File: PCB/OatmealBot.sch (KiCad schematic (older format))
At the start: 30 parts, among them J1 ServoHeader1, J10 ServoHeader3, J11 ServoHeader3, J12 ServoHeader3, J2 RPi_GPIO, J3 ServoHeader2, J4 ServoHeader1, J5 Motor 3, J6 Motor 4, J7 ServoHeader2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

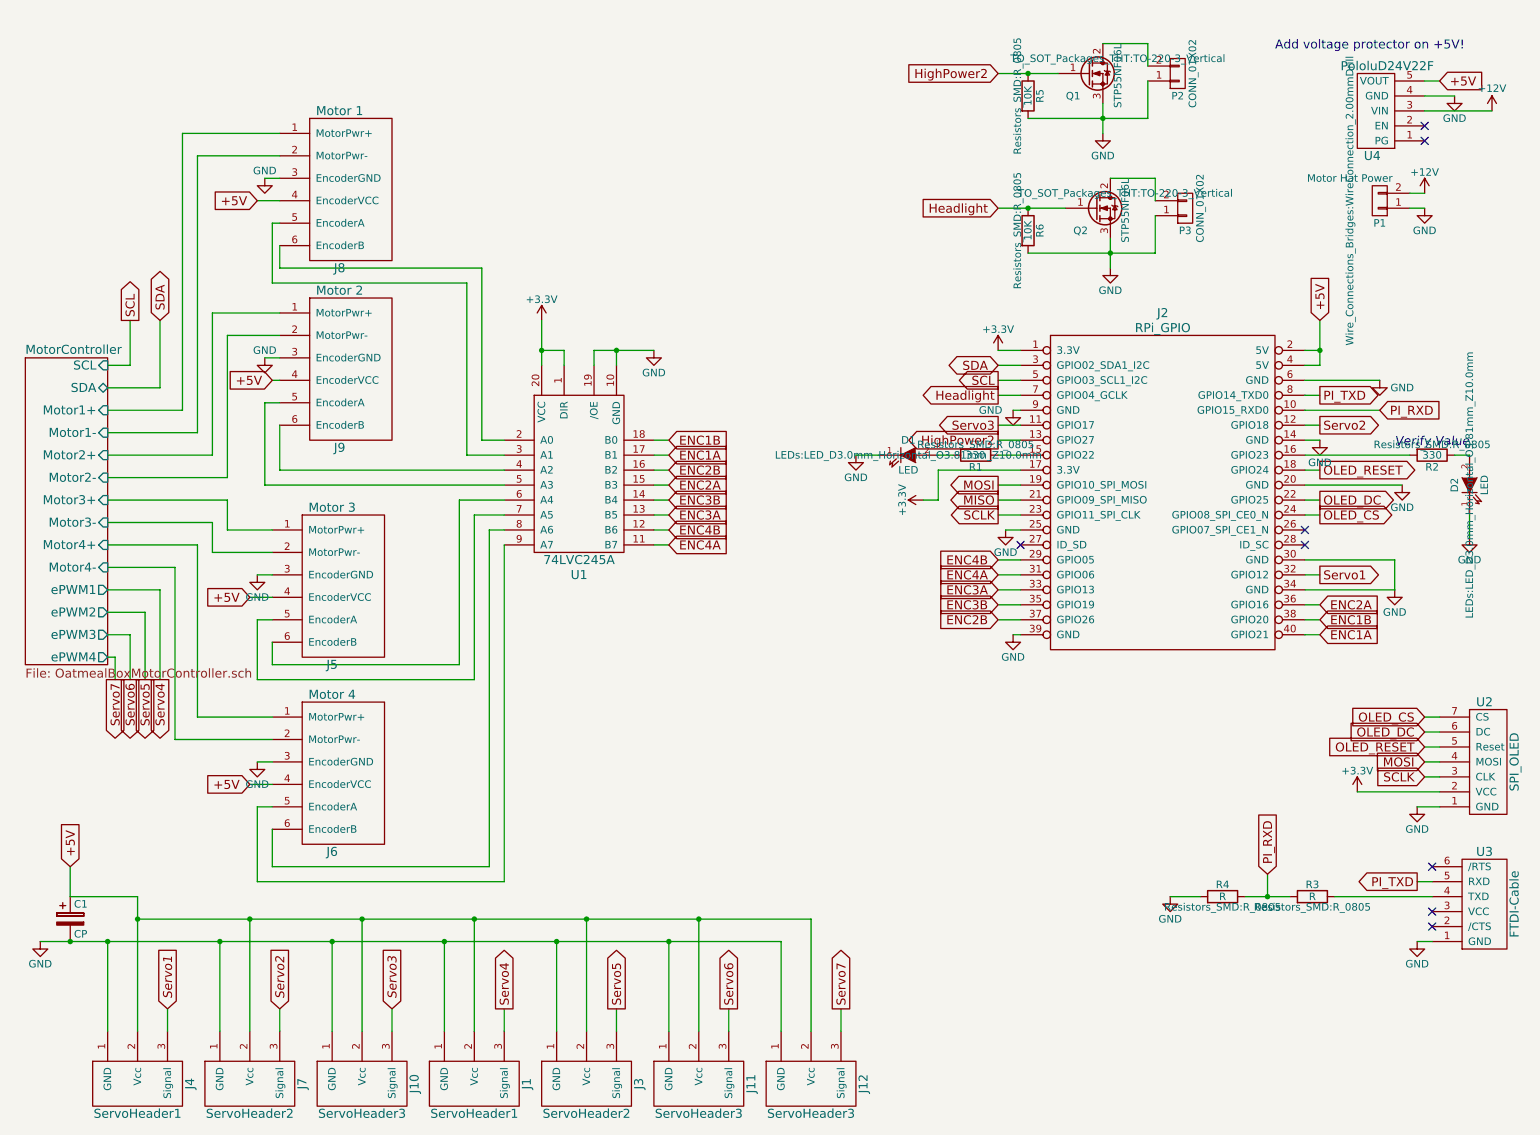
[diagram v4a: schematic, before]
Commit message: Cleaned up, renamed a few things and added all footprints.
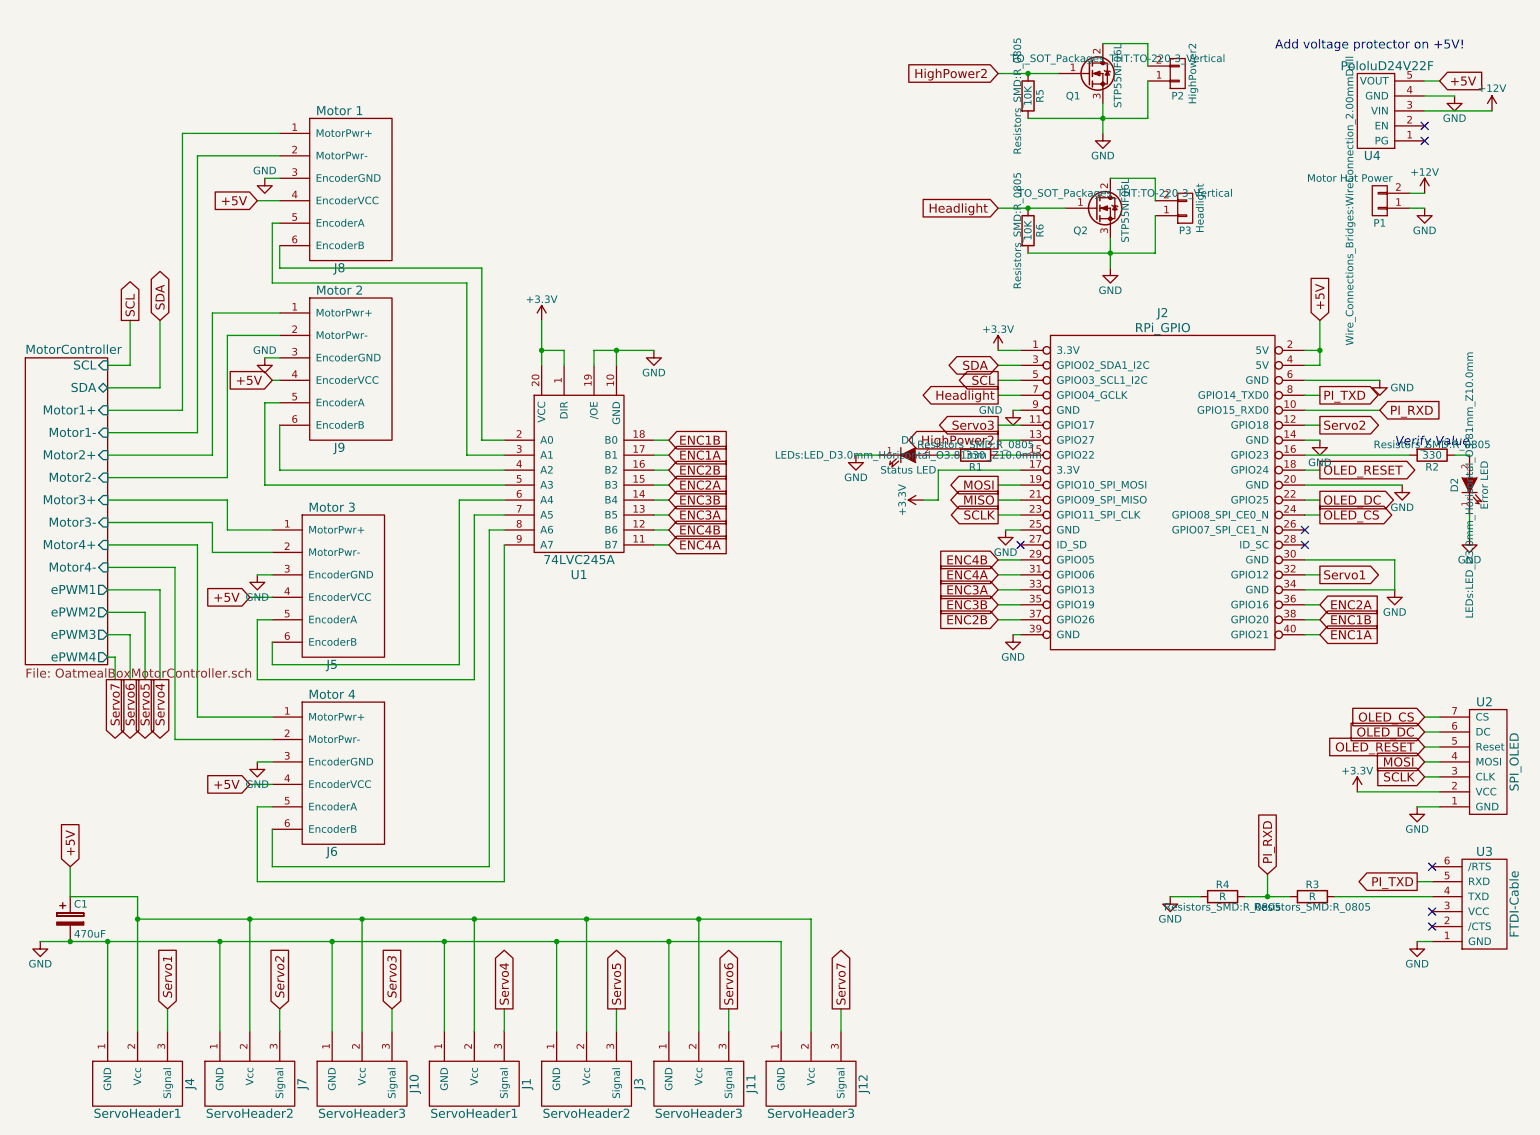
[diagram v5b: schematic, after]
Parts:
- C1: value CP -> 470uF; footprint (none) -> Capacitors_ThroughHole:CP_Radial_D12.5mm_P5.00mm
- D1: value LED -> Status LED
- D2: value LED -> Error LED
- P2: value CONN_01X02 -> HighPower2; footprint (none) -> Pin_Headers:Pin_Header_Straight_1x02_Pitch2.54mm
- P3: value CONN_01X02 -> Headlight; footprint (none) -> Pin_Headers:Pin_Header_Straight_1x02_Pitch2.54mm
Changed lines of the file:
@@
 +5V
 $Comp
-L GND #PWR4
+L GND #PWR01
 U 1 1 5B1F57E8
 P 2100 1450
-F 0 "#PWR4" H 2100 1200 50  0001 C CNN
+F 0 "#PWR01" H 2100 1200 50  0001 C CNN
 F 1 "GND" H 2100 1500 50  0000 C CNN
 F 2 "" H 2100 1450 50  0000 C CNN
@@
 +5V
 $Comp
-L GND #PWR5
+L GND #PWR02
 U 1 1 5B1F5859
 P 2100 2650
-F 0 "#PWR5" H 2100 2400 50  0001 C CNN
+F 0 "#PWR02" H 2100 2400 50  0001 C CNN
 F 1 "GND" H 2100 2700 50  0000 C CNN
 F 2 "" H 2100 2650 50  0000 C CNN
@@
 	1750 2350 2200 2350
 $Comp
-L GND #PWR3
+L GND #PWR03
 U 1 1 5B20546D
 P 2050 5350
-F 0 "#PWR3" H 2050 5100 50  0001 C CNN
+F 0 "#PWR03" H 2050 5100 50  0001 C CNN
 F 1 "GND" H 2050 5200 50  0000 C CNN
 F 2 "" H 2050 5350 50  0000 C CNN
@@
 $EndComp
 $Comp
-L GND #PWR2
+L GND #PWR04
 U 1 1 5B2054AE
 P 2050 4100
-F 0 "#PWR2" H 2050 3850 50  0001 C CNN
+F 0 "#PWR04" H 2050 3850 50  0001 C CNN
 F 1 "GND" H 2050 3950 50  0000 C CNN
 F 2 "" H 2050 4100 50  0000 C CNN
@@
 $EndComp
 $Comp
-L GND #PWR7
+L GND #PWR05
 U 1 1 5B24A42D
 P 4700 2600
-F 0 "#PWR7" H 4700 2350 50  0001 C CNN
+F 0 "#PWR05" H 4700 2350 50  0001 C CNN
 F 1 "GND" H 4700 2450 50  0000 C CNN
 F 2 "" H 4700 2600 50  0000 C CNN
@@
 P 10150 3500
 F 0 "D2" H 10150 3600 50  0000 C CNN
-F 1 "LED" H 10150 3400 50  0000 C CNN
+F 1 "Error LED" H 10150 3400 50  0000 C CNN
 F 2 "LEDs:LED_D3.0mm_Horizontal_O3.81mm_Z10.0mm" H 10150 3500 50  0000 C CNN
 F 3 "" H 10150 3500 50  0000 C CNN
@@
 P 6400 3300
 F 0 "D1" H 6400 3400 50  0000 C CNN
-F 1 "LED" H 6400 3200 50  0000 C CNN
+F 1 "Status LED" H 6400 3200 50  0000 C CNN
 F 2 "LEDs:LED_D3.0mm_Horizontal_O3.81mm_Z10.0mm" H 6400 3300 50  0000 C CNN
 F 3 "" H 6400 3300 50  0000 C CNN
@@
 $EndComp
 $Comp
-L GND #PWR27
+L GND #PWR06
 U 1 1 5B24C448
 P 10150 3850
-F 0 "#PWR27" H 10150 3600 50  0001 C CNN
+F 0 "#PWR06" H 10150 3600 50  0001 C CNN
 F 1 "GND" H 10150 3700 50  0000 C CNN
 F 2 "" H 10150 3850 50  0000 C CNN
@@
 $EndComp
 $Comp
-L GND #PWR8
+L GND #PWR07
 U 1 1 5B24C48C
 P 6050 3300
-F 0 "#PWR8" H 6050 3050 50  0001 C CNN
+F 0 "#PWR07" H 6050 3050 50  0001 C CNN
 F 1 "GND" H 6050 3150 50  0000 C CNN
 F 2 "" H 6050 3300 50  0000 C CNN
@@
 $EndComp
 $Comp
-L GND #PWR1
+L GND #PWR08
 U 1 1 5B24CDE6
 P 600 6550
-F 0 "#PWR1" H 600 6300 50  0001 C CNN
+F 0 "#PWR08" H 600 6300 50  0001 C CNN
 F 1 "GND" H 600 6400 50  0000 C CNN
 F 2 "" H 600 6550 50  0000 C CNN
@@
 $EndComp
 $Comp
-L GND #PWR26
+L GND #PWR09
 U 1 1 5B28887D
 P 10050 900
-F 0 "#PWR26" H 10050 650 50  0001 C CNN
+F 0 "#PWR09" H 10050 650 50  0001 C CNN
 F 1 "GND" H 10050 750 50  0000 C CNN
 F 2 "" H 10050 900 50  0000 C CNN
@@
 $EndComp
 $Comp
-L GND #PWR25
+L GND #PWR010
 U 1 1 5B2897C9
 P 9850 1650
-F 0 "#PWR25" H 9850 1400 50  0001 C CNN
+F 0 "#PWR010" H 9850 1400 50  0001 C CNN
 F 1 "GND" H 9850 1500 50  0000 C CNN
 F 2 "" H 9850 1650 50  0000 C CNN
@@
 $EndComp
 $Comp
-L +12V #PWR24
+L +12V #PWR011
 U 1 1 5B289821
 P 9850 1550
-F 0 "#PWR24" H 9850 1400 50  0001 C CNN
+F 0 "#PWR011" H 9850 1400 50  0001 C CNN
 F 1 "+12V" H 9850 1690 50  0000 C CNN
 F 2 "" H 9850 1550 50  0000 C CNN
@@
 	9750 1650 9850 1650
 $Comp
-L +12V #PWR28
+L +12V #PWR012
 U 1 1 5B289B43
 P 10300 1000
-F 0 "#PWR28" H 10300 850 50  0001 C CNN
+F 0 "#PWR012" H 10300 850 50  0001 C CNN
 F 1 "+12V" H 10300 1150 50  0000 C CNN
 F 2 "" H 10300 1000 50  0000 C CNN
@@
 $EndComp
 $Comp
-L GND #PWR23
+L GND #PWR013
 U 1 1 5B299D08
 P 9800 6550
-F 0 "#PWR23" H 9800 6300 50  0001 C CNN
+F 0 "#PWR013" H 9800 6300 50  0001 C CNN
 F 1 "GND" H 9800 6400 50  0000 C CNN
 F 2 "" H 9800 6550 50  0000 C CNN
@@
 $EndComp
 $Comp
-L GND #PWR16
+L GND #PWR014
 U 1 1 5B29AF0F
 P 8150 6250
-F 0 "#PWR16" H 8150 6000 50  0001 C CNN
+F 0 "#PWR014" H 8150 6000 50  0001 C CNN
 F 1 "GND" H 8150 6100 50  0000 C CNN
 F 2 "" H 8150 6250 50  0000 C CNN
@@
 $EndComp
 $Comp
-L GND #PWR22
+L GND #PWR015
 U 1 1 5B29A611
 P 9800 5650
-F 0 "#PWR22" H 9800 5400 50  0001 C CNN
+F 0 "#PWR015" H 9800 5400 50  0001 C CNN
 F 1 "GND" H 9800 5500 50  0000 C CNN
 F 2 "" H 9800 5650 50  0000 C CNN
@@
 $EndComp
 $Comp
-L +3.3V #PWR18
+L +3.3V #PWR016
 U 1 1 5B29B07B
 P 9400 5550
-F 0 "#PWR18" H 9400 5400 50  0001 C CNN
+F 0 "#PWR016" H 9400 5400 50  0001 C CNN
 F 1 "+3.3V" H 9400 5690 50  0000 C CNN
 F 2 "" H 9400 5550 50  0000 C CNN
@@
 NoConn ~ 9850 1200
 $Comp
-L GND #PWR20
+L GND #PWR017
 U 1 1 5B2CC2C8
 P 9650 4200
-F 0 "#PWR20" H 9650 3950 50  0001 C CNN
+F 0 "#PWR017" H 9650 3950 50  0001 C CNN
 F 1 "GND" H 9650 4050 50  0000 C CNN
 F 2 "" H 9650 4200 50  0000 C CNN
@@
 	9050 4200 9650 4200
 $Comp
-L GND #PWR17
+L GND #PWR018
 U 1 1 5B2CC630
 P 9150 3200
-F 0 "#PWR17" H 9150 2950 50  0001 C CNN
+F 0 "#PWR018" H 9150 2950 50  0001 C CNN
 F 1 "GND" H 9150 3050 50  0000 C CNN
 F 2 "" H 9150 3200 50  0000 C CNN
@@
 $EndComp
 $Comp
-L GND #PWR19
+L GND #PWR019
 U 1 1 5B2CC794
 P 9550 2800
-F 0 "#PWR19" H 9550 2550 50  0001 C CNN
+F 0 "#PWR019" H 9550 2550 50  0001 C CNN
 F 1 "GND" H 9700 2750 50  0000 C CNN
 F 2 "" H 9550 2800 50  0000 C CNN
@@
 Connection ~ 9150 2600
 $Comp
-L GND #PWR21
+L GND #PWR020
 U 1 1 5B2CD7F6
 P 9700 3500
-F 0 "#PWR21" H 9700 3250 50  0001 C CNN
+F 0 "#PWR020" H 9700 3250 50  0001 C CNN
 F 1 "GND" H 9700 3350 50  0000 C CNN
 F 2 "" H 9700 3500 50  0000 C CNN
@@
 	7150 3100 7000 3100
 $Comp
-L GND #PWR13
+L GND #PWR021
 U 1 1 5B2D3626
 P 7100 4500
-F 0 "#PWR13" H 7100 4250 50  0001 C CNN
+F 0 "#PWR021" H 7100 4250 50  0001 C CNN
 F 1 "GND" H 7100 4350 50  0000 C CNN
 F 2 "" H 7100 4500 50  0000 C CNN
@@
 $EndComp
 $Comp
-L GND #PWR12
+L GND #PWR022
 U 1 1 5B2D368E
 P 7100 3000
-F 0 "#PWR12" H 7100 2750 50  0001 C CNN
+F 0 "#PWR022" H 7100 2750 50  0001 C CNN
 F 1 "GND" H 6950 3000 50  0000 C CNN
 F 2 "" H 7100 3000 50  0000 C CNN
@@
 $EndComp
 $Comp
-L GND #PWR11
+L GND #PWR023
 U 1 1 5B2D3A13
 P 7050 3800
-F 0 "#PWR11" H 7050 3550 50  0001 C CNN
+F 0 "#PWR023" H 7050 3550 50  0001 C CNN
 F 1 "GND" H 7050 3650 50  0000 C CNN
 F 2 "" H 7050 3800 50  0000 C CNN
@@
 $EndComp
 $Comp
-L GND #PWR15
+L GND #PWR024
 U 1 1 5B37B1D3
 P 7750 2050
-F 0 "#PWR15" H 7750 1800 50  0001 C CNN
+F 0 "#PWR024" H 7750 1800 50  0001 C CNN
 F 1 "GND" H 7750 1900 50  0000 C CNN
 F 2 "" H 7750 2050 50  0000 C CNN
@@
 P 8250 1650
 F 0 "P3" H 8250 1800 50  0000 C CNN
-F 1 "CONN_01X02" V 8350 1650 50  0000 C CNN
-F 2 "" H 8250 1650 50  0000 C CNN
+F 1 "Headlight" V 8350 1650 50  0000 C CNN
+F 2 "Pin_Headers:Pin_Header_Straight_1x02_Pitch2.54mm" H 8250 1650 50  0001 C CNN
 F 3 "" H 8250 1650 50  0000 C CNN
 	1    8250 1650
@@
 P 8200 750
 F 0 "P2" H 8200 900 50  0000 C CNN
-F 1 "CONN_01X02" V 8300 750 50  0000 C CNN
-F 2 "" H 8200 750 50  0000 C CNN
+F 1 "HighPower2" V 8300 750 50  0000 C CNN
+F 2 "Pin_Headers:Pin_Header_Straight_1x02_Pitch2.54mm" H 8200 750 50  0001 C CNN
 F 3 "" H 8200 750 50  0000 C CNN
 	1    8200 750
@@
 $EndComp
 $Comp
-L GND #PWR14
+L GND #PWR025
 U 1 1 5B3875B5
 P 7700 1150
-F 0 "#PWR14" H 7700 900 50  0001 C CNN
+F 0 "#PWR025" H 7700 900 50  0001 C CNN
 F 1 "GND" H 7700 1000 50  0000 C CNN
 F 2 "" H 7700 1150 50  0000 C CNN
@@
 P 800 6400
 F 0 "C1" H 825 6500 50  0000 L CNN
-F 1 "CP" H 825 6300 50  0000 L CNN
-F 2 "" H 838 6250 50  0001 C CNN
+F 1 "470uF" H 825 6300 50  0000 L CNN
+F 2 "Capacitors_ThroughHole:CP_Radial_D12.5mm_P5.00mm" H 838 6250 50  0001 C CNN
 F 3 "" H 800 6400 50  0001 C CNN
 	1    800  6400
@@
 	1200 4500 1200 4800
 $Comp
-L +3.3V #PWR10
+L +3.3V #PWR026
 U 1 1 5B4FAF00
 P 7000 2600
-F 0 "#PWR10" H 7000 2450 50  0001 C CNN
+F 0 "#PWR026" H 7000 2450 50  0001 C CNN
 F 1 "+3.3V" H 7000 2740 50  0000 C CNN
 F 2 "" H 7000 2600 50  0001 C CNN
@@
 	1400 2850 1400 2400
 $Comp
-L +3.3V #PWR6
+L +3.3V #PWR027
 U 1 1 5B503843
 P 3950 2400
-F 0 "#PWR6" H 3950 2250 50  0001 C CNN
+F 0 "#PWR027" H 3950 2250 50  0001 C CNN
 F 1 "+3.3V" H 3950 2540 50  0000 C CNN
 F 2 "" H 3950 2400 50  0001 C CNN
@@
 NoConn ~ 9050 3800
 $Comp
-L +3.3V #PWR9
+L +3.3V #PWR028
 U 1 1 5B5043F5
 P 6500 3600
-F 0 "#PWR9" H 6500 3450 50  0001 C CNN
+F 0 "#PWR028" H 6500 3450 50  0001 C CNN
 F 1 "+3.3V" H 6500 3740 50  0000 C CNN
 F 2 "" H 6500 3600 50  0001 C CNN
